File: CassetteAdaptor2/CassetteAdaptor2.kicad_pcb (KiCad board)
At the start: 2 copper layers, 37.6 x 30 mm, 3 parts, among them J1 Cassette, J2 CS1 EAR, J3 CS1 MIC

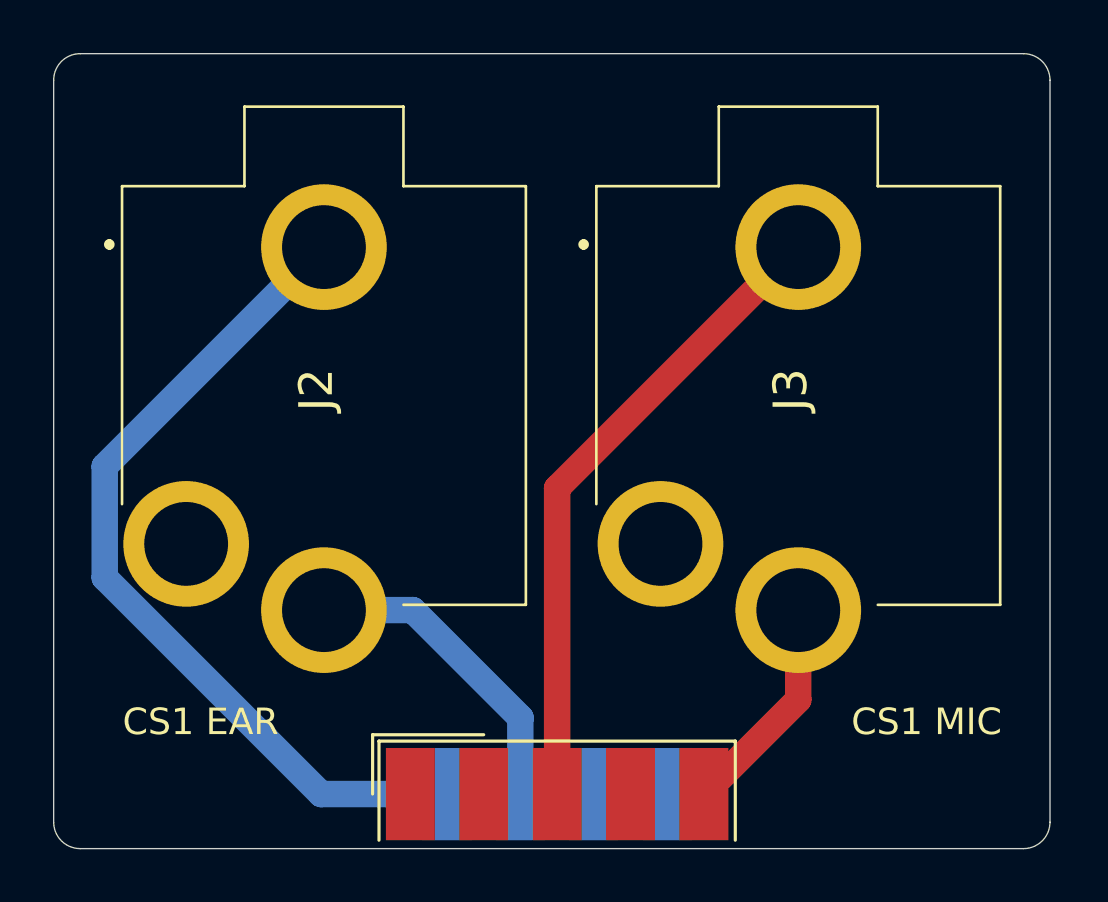
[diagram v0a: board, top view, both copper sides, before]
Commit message: PCBs fabricated for testing
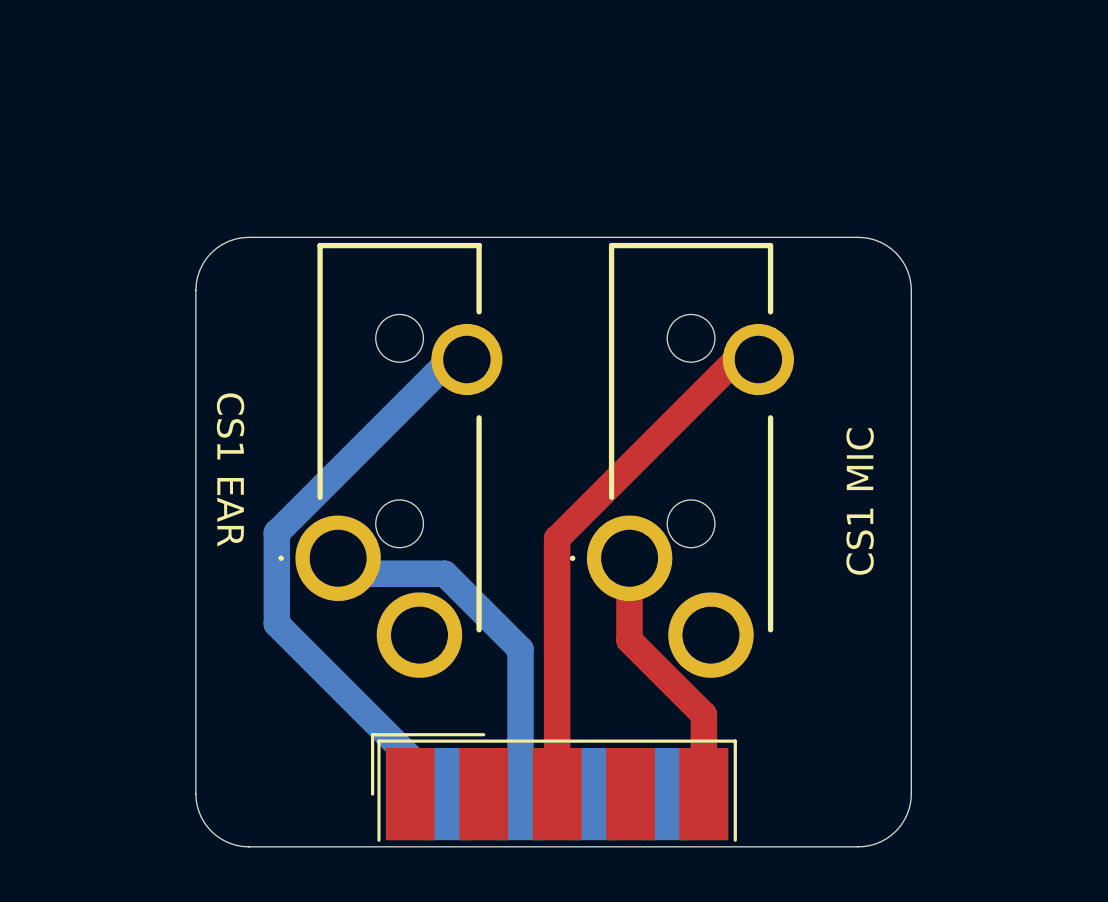
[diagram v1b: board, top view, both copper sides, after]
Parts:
- J2, J3: footprint Clueless_Engineer:MJ3536N -> Clueless_Engineer:SJ3350820BTR
- moved J3 8.79 mm to (99.7, 61.3)
- moved J2 6.41 mm to (88.7, 61.3)
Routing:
- net CS1_EAR-: track 32.2 -> 22.4 mm
- net CS1_MIC-: track 24.4 -> 20.0 mm
- net CS1_EAR+: track 12.0 -> 13.8 mm
- net CS1_MIC+: track 8.42 -> 10.1 mm
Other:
- board size 37.6 x 30 mm -> 27 x 23 mm
- board text added: "TI 99/4A Cassette Rev. B"
- board text removed: "TI 99/4A Cassette"
